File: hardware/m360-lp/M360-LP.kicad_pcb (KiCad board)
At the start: 2 copper layers, 0 parts

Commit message: feat(hardware): footprints da família e posicionamento da M360-LP na caixa
Biblioteca hardware/lib/M360.pretty com os quatro footprints que faltavam: Pro Mini,
soquete do mezanino, RJ45 (C385834) e reed (C315909). Os dois últimos vieram do LCSC pelo
easyeda2kicad, com os pinos-guia do RJ45 corrigidos para furo não metalizado e o modelo 3D
subido 6,3 mm — vinha atravessando a placa. O datasheet confirma conector comum: corpo de
12,6 mm apoiado na face e pinos de 3,0 mm.

O soquete do mezanino não precisa ser espelhado: o PinSocket stock já tem a coluna par em x
negativo, o mesmo lado em que ela fica no J1 do mezanino, que é montado na face de baixo.
Esquemático e documento corrigidos.

Furos livres do Pro Mini medidos por foto (docs/prominiFront.jpg), por homografia a partir
de quatro pinos de canto de posição conhecida (passo 2,54 mm, fileiras a 15,24 mm; escala
consistente em 2% nas quatro bordas): A5 em (12,70; 8,89), A4 em (12,70; 11,43) e GND/A6/A7
em x = 7,62/10,16/12,70 com y = 28,3 ± 0,3. Os espaçamentos medidos (2,57 e 2,59 mm)
confirmam a grade de 2,54. Esses cinco furos levam 1,2 mm — e não 1,0 — para absorver a
incerteza da medição; confirmar com paquímetro antes de fabricar.

Posicionamento em 86 × 62 mm, formato imposto pela caixa de 100 × 100 × 50 mm: o plugue
RJ45 é crimpado dentro da caixa e pede ~25-30 mm livres à frente dos conectores, com os
prensa-cabos na parede em frente. RJ45 e reed na borda de baixo, TVS logo atrás deles,
matriz RC dos 8 canais no meio, Pro Mini deitado com o header FTDI para fora da borda
esquerda, mezanino no alto à direita com o SMA pela borda e a alimentação embaixo dele
(~11 mm livres, só SMD baixo). DRC sem sobreposição de courtyard nem erro de isolamento;
faltam o roteamento e o acerto de serigrafia dos textos de U2, U4 e U5.

Co-Authored-By: Claude Opus 5 (1M context) <noreply@anthropic.com>
Claude-Session: https://claude.ai/code/session_01G3CpSsqAsoKgMUYE5MhRV7
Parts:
- added A1: Pro Mini 3V3 8MHz, M360:Arduino_ProMini_DeeKRobot, F.Cu at (112.0, 121.0)
- added C1: 1uF, Capacitor_SMD:C_0603_1608Metric, F.Cu at (169.5, 104.0)
- added C10: 100nF, Capacitor_SMD:C_0603_1608Metric, F.Cu at (114.4, 139.5)
- added C11: 100nF, Capacitor_SMD:C_0603_1608Metric, F.Cu at (118.6, 139.5)
- added C12: 100nF, Capacitor_SMD:C_0603_1608Metric, F.Cu at (122.8, 139.5)
- added C13: 100nF, Capacitor_SMD:C_0603_1608Metric, F.Cu at (127.0, 139.5)
- added C14: 100nF, Capacitor_SMD:C_0603_1608Metric, F.Cu at (131.2, 139.5)
- added C15: 100nF, Capacitor_SMD:C_0603_1608Metric, F.Cu at (135.4, 139.5)
- added C2: 1uF, Capacitor_SMD:C_0603_1608Metric, F.Cu at (178.0, 104.0)
- added C3: 10uF, Capacitor_SMD:C_0805_2012Metric, F.Cu at (165.0, 116.0)
- added C4: 100nF, Capacitor_SMD:C_0603_1608Metric, F.Cu at (142.0, 125.5)
- added C5: 10nF, Capacitor_SMD:C_0603_1608Metric, F.Cu at (172.5, 110.0)
- added C6: 1uF, Capacitor_SMD:C_0603_1608Metric, F.Cu at (178.5, 110.0)
- added C7: 100nF, Capacitor_SMD:C_0603_1608Metric, F.Cu at (147.0, 105.5)
- added C8: 100nF, Capacitor_SMD:C_0603_1608Metric, F.Cu at (106.0, 139.5)
- added C9: 100nF, Capacitor_SMD:C_0603_1608Metric, F.Cu at (110.2, 139.5)
- added H1: MountingHole_3.2mm_M3, MountingHole_3.2mm_M3, F.Cu at (103.5, 103.5)
- added H2: MountingHole_3.2mm_M3, MountingHole_3.2mm_M3, F.Cu at (182.5, 128.0)
- added H3: MountingHole_3.2mm_M3, MountingHole_3.2mm_M3, F.Cu at (103.5, 158.5)
- added H4: MountingHole_3.2mm_M3, MountingHole_3.2mm_M3, F.Cu at (182.5, 158.5)
- added J1: RJ45 SOLO, M360:RJ45_R-RJ45R08P-A004, F.Cu at (116.0, 153.3)
- added J2: RJ45 CLIMA/AUX, M360:RJ45_R-RJ45R08P-A004, F.Cu at (134.0, 153.3)
- added J3: J_VIN 3,0-6V, Connector_JST:JST_XH_B2B-XH-A_1x02_P2.50mm_Vertical, F.Cu at (178.0, 140.0)
- added J4: M360-RF, M360:M360-RF_Soquete_2x05, F.Cu at (158.8, 107.4)
- added Q1: AO3401A, Package_TO_SOT_SMD:SOT-23, F.Cu at (165.0, 104.0)
- added Q2: AO3401A, Package_TO_SOT_SMD:SOT-23, F.Cu at (165.0, 110.0)
- added R1: 2M, Resistor_SMD:R_0603_1608Metric, F.Cu at (134.0, 125.5)
- added R10: 10k, Resistor_SMD:R_0603_1608Metric, F.Cu at (122.8, 129.5)
- added R11: 10k, Resistor_SMD:R_0603_1608Metric, F.Cu at (127.0, 129.5)
- added R12: 10k, Resistor_SMD:R_0603_1608Metric, F.Cu at (131.2, 129.5)
- added R13: 10k, Resistor_SMD:R_0603_1608Metric, F.Cu at (135.4, 129.5)
- added R14: 1k, Resistor_SMD:R_0603_1608Metric, F.Cu at (106.0, 134.5)
- added R15: 1k, Resistor_SMD:R_0603_1608Metric, F.Cu at (110.2, 134.5)
- added R16: 1k, Resistor_SMD:R_0603_1608Metric, F.Cu at (114.4, 134.5)
- added R17: 1k, Resistor_SMD:R_0603_1608Metric, F.Cu at (118.6, 134.5)
- added R18: 1k, Resistor_SMD:R_0603_1608Metric, F.Cu at (122.8, 134.5)
- added R19: 1k, Resistor_SMD:R_0603_1608Metric, F.Cu at (127.0, 134.5)
- added R2: 1M, Resistor_SMD:R_0603_1608Metric, F.Cu at (138.0, 125.5)
- added R20: 1k, Resistor_SMD:R_0603_1608Metric, F.Cu at (131.2, 134.5)
- added R21: 1k, Resistor_SMD:R_0603_1608Metric, F.Cu at (135.4, 134.5)
- added R22: 4.7k, Resistor_SMD:R_0603_1608Metric, F.Cu at (155.0, 130.0)
- added R23: 10k, Resistor_SMD:R_0603_1608Metric, F.Cu at (159.0, 130.0)
- added R24: 3.3k, Resistor_SMD:R_0603_1608Metric, F.Cu at (163.0, 130.0)
- added R25: 3.3k, Resistor_SMD:R_0603_1608Metric, F.Cu at (167.0, 130.0)
- added R3: 10k, Resistor_SMD:R_0603_1608Metric, F.Cu at (147.0, 118.5)
- added R4: 100k, Resistor_SMD:R_0603_1608Metric, F.Cu at (169.5, 110.0)
- added R5: 10k, Resistor_SMD:R_0603_1608Metric, F.Cu at (175.5, 110.0)
- added R6: 10k, Resistor_SMD:R_0603_1608Metric, F.Cu at (106.0, 129.5)
- added R7: 10k, Resistor_SMD:R_0603_1608Metric, F.Cu at (110.2, 129.5)
- added R8: 10k, Resistor_SMD:R_0603_1608Metric, F.Cu at (114.4, 129.5)
- added R9: 10k, Resistor_SMD:R_0603_1608Metric, F.Cu at (118.6, 129.5)
- added SW1: Reed, M360:Reed_Littelfuse_59170, F.Cu at (160.0, 158.0)
- added U1: MCP1700T-3302E/TT, Package_TO_SOT_SMD:SOT-23, F.Cu at (174.0, 104.0)
- added U2: 74HC4051, Package_SO:SOIC-16_3.9x9.9mm_P1.27mm, F.Cu at (147.0, 112.0)
- added U3: SRV05-4, Package_TO_SOT_SMD:SOT-23-6, F.Cu at (112.0, 143.5)
- added U4: SRV05-4, Package_TO_SOT_SMD:SOT-23-6, F.Cu at (124.0, 143.5)
- added U5: SRV05-4, Package_TO_SOT_SMD:SOT-23-6, F.Cu at (136.0, 143.5)
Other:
- board outline added: 86 x 62 mm

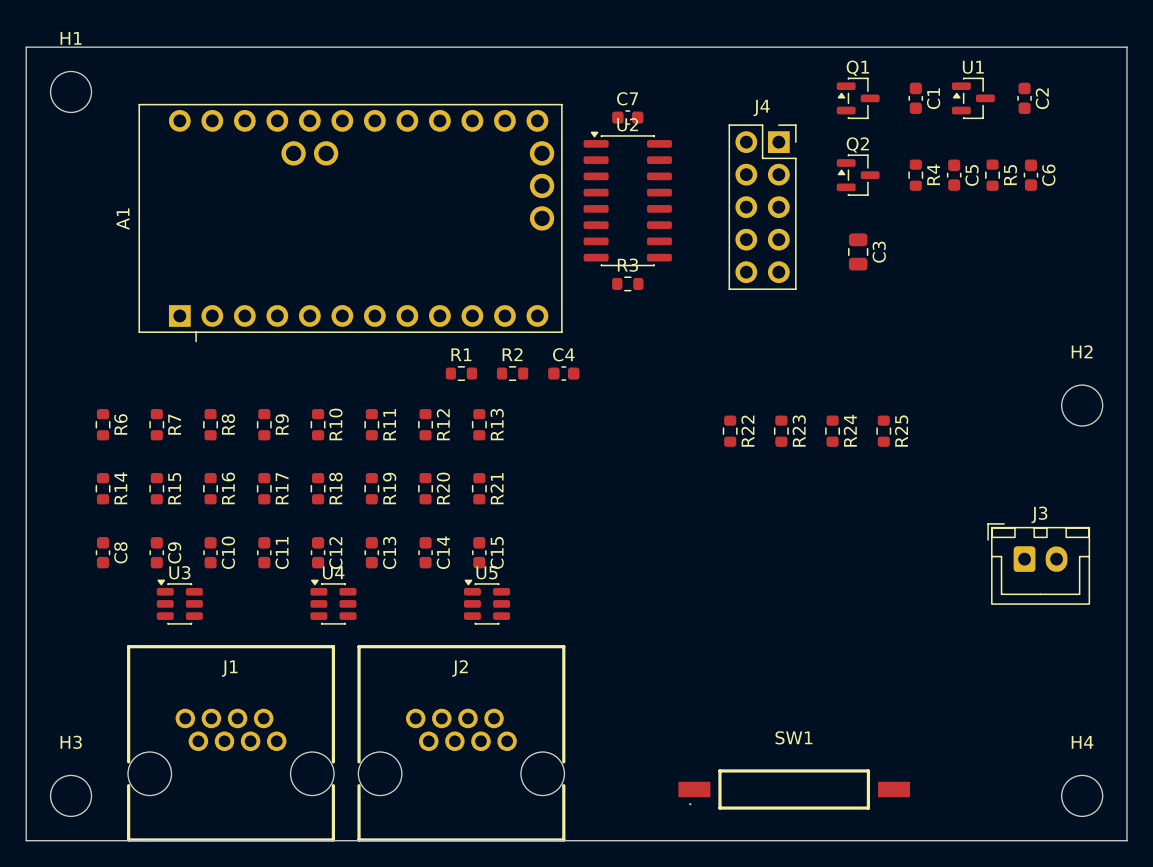
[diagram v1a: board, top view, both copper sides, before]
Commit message: feat(hardware): roteamento e planos de terra da M360-LP
Regras da placa antes de rotear: isolamento 0,2 mm, trilha 0,25 mm e via 0,6/0,3 mm
(estavam em isolamento 0 e trilha 0,2).

Roteamento pelo Freerouting 1.9.0, chamado direto na linha de comando: o autoroute do MCP
exige Java 21 ou Docker em execução, e aqui há Java 17 — que basta para a versão 1.9.
Fluxo: export DSN pelo MCP, `java -jar freerouting.jar -de ... -do ... -mp 20`, import SES
pelo MCP. Resultado: 552 trilhas e 48 vias, com a otimização melhorando o desenho em ~51%.
**Zero ligações pendentes** (eram 135) e nenhuma violação de isolamento.

Planos de terra (GND) nas duas faces, isolamento de 0,25 mm, preenchidos com
`kicad-cli pcb drc --refill-zones --save-board` — o refill_zones do MCP é o que arrisca
falha de segmentação.

Dois erros de haste térmica insuficiente apareceram com o preenchimento e foram corrigidos:
- hastes de 0,35 mm com folga de 0,3 mm (eram 0,5/0,5), que cabem no anel apertado dos pads
  THT e preservam o alívio térmico para a solda manual — resolveu o pino 10 do J4;
- ligação sólida no pino 8 do J2 (GND do RJ45), onde o campo de pinos escalonados de
  1,02 mm não deixa espaço para duas hastes. É o pad de terra do chicote: ligação sólida dá
  o melhor retorno de massa, ao custo de mais calor na solda desse pad.

Restam apenas avisos de serigrafia: a frente dos RJ45 rente à borda (proposital) e textos de
referência de U2, U4 e U5 sobre ilhas — acerto cosmético pendente.

Co-Authored-By: Claude Opus 5 (1M context) <noreply@anthropic.com>
Claude-Session: https://claude.ai/code/session_01G3CpSsqAsoKgMUYE5MhRV7
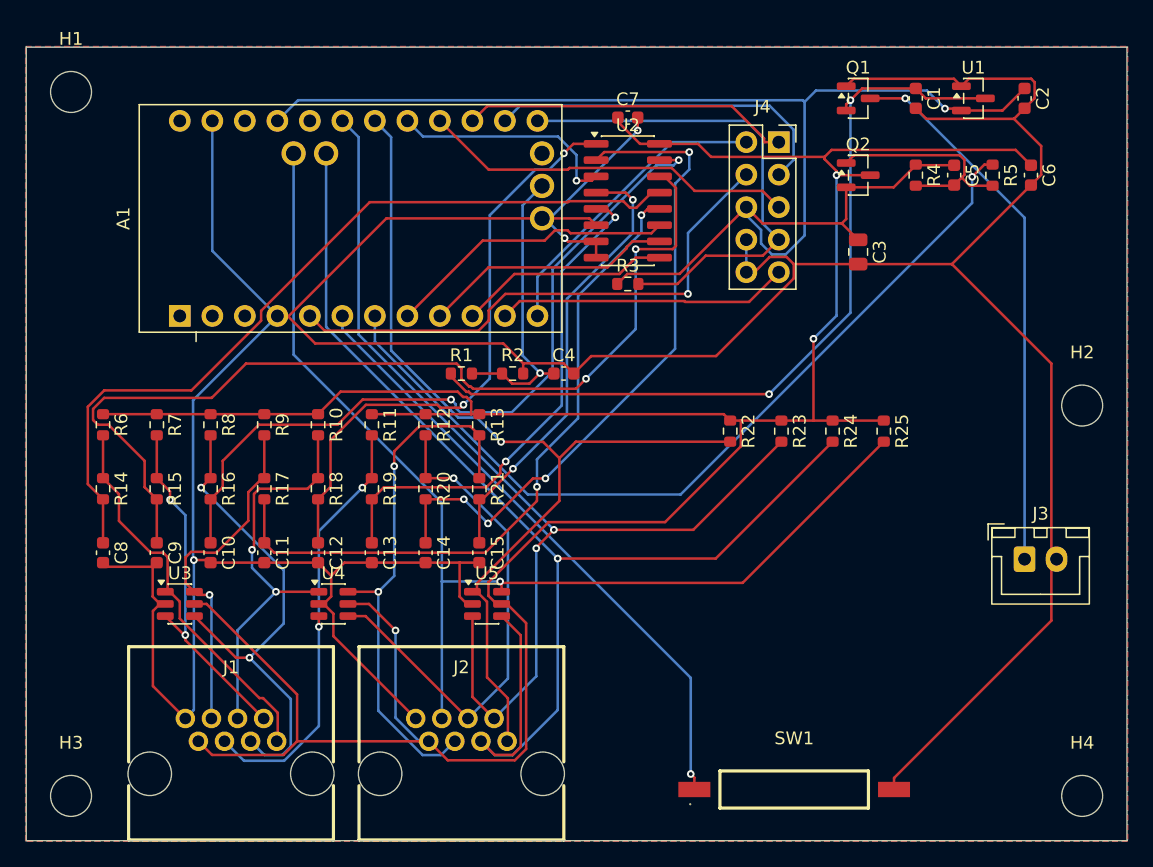
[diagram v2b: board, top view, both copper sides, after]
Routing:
- net GND: track 0.00 -> 315.2 mm, vias 0 -> 3
- net VSW: track 0.00 -> 227.5 mm, vias 0 -> 3
- net 3V3: track 0.00 -> 113.5 mm, vias 0 -> 1
- net SDA: track 0.00 -> 98.8 mm, vias 0 -> 1
- net SCL: track 0.00 -> 88.8 mm, vias 0 -> 1
- net DHT: track 0.00 -> 84.8 mm, vias 0 -> 2
- net SOIL1_F: track 0.00 -> 75.8 mm, vias 0 -> 2
- net ONEWIRE: track 0.00 -> 75.1 mm, vias 0 -> 1
- net VSW_EN: track 0.00 -> 67.1 mm, vias 0 -> 1
- net SOIL0_F: track 0.00 -> 63.6 mm
- net VIN: track 0.00 -> 63.4 mm, vias 0 -> 2
- net SOIL2_F: track 0.00 -> 59.4 mm, vias 0 -> 2
- net SOIL3_F: track 0.00 -> 54.0 mm, vias 0 -> 2
- net SOIL6_F: track 0.00 -> 52.7 mm, vias 0 -> 4
- net REED: track 0.00 -> 48.4 mm, vias 0 -> 1
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- added copper zone on B.Cu, net GND
- added copper zone on F.Cu, net GND

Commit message: feat(hardware): serigrafia da M360-LP e marca da placa
Os textos de referência de U2, U4 e U5 caíam sobre os pads de C7, C12 e C15, e o do R3 sobre
o contorno de serigrafia do U2 — os oito avisos de componente que sobraram do roteamento. Os
textos foram movidos para a folga livre ao lado de cada peça; nenhum componente mudou de
lugar, então o roteamento não foi tocado:

- U2 vai para a folga entre o corpo e o soquete do mezanino, na vertical;
- U4 e U5 vão para o vão à direita de cada um, entre os TVS e os pull-ups;
- R3 desce para baixo do próprio corpo, saindo do contorno do U2.

Acrescentado "Viridiotech.com.br" na face de cima, no espaço vazio acima do SW1, com 1,5 mm
de altura.

Continuam os oito avisos da frente dos RJ45 rente à borda: são propositais, porque a boca do
conector fica na borda da placa, e a serigrafia ali é aparada na fabricação.

Co-Authored-By: Claude Opus 5 (1M context) <noreply@anthropic.com>
Claude-Session: https://claude.ai/code/session_01G3CpSsqAsoKgMUYE5MhRV7
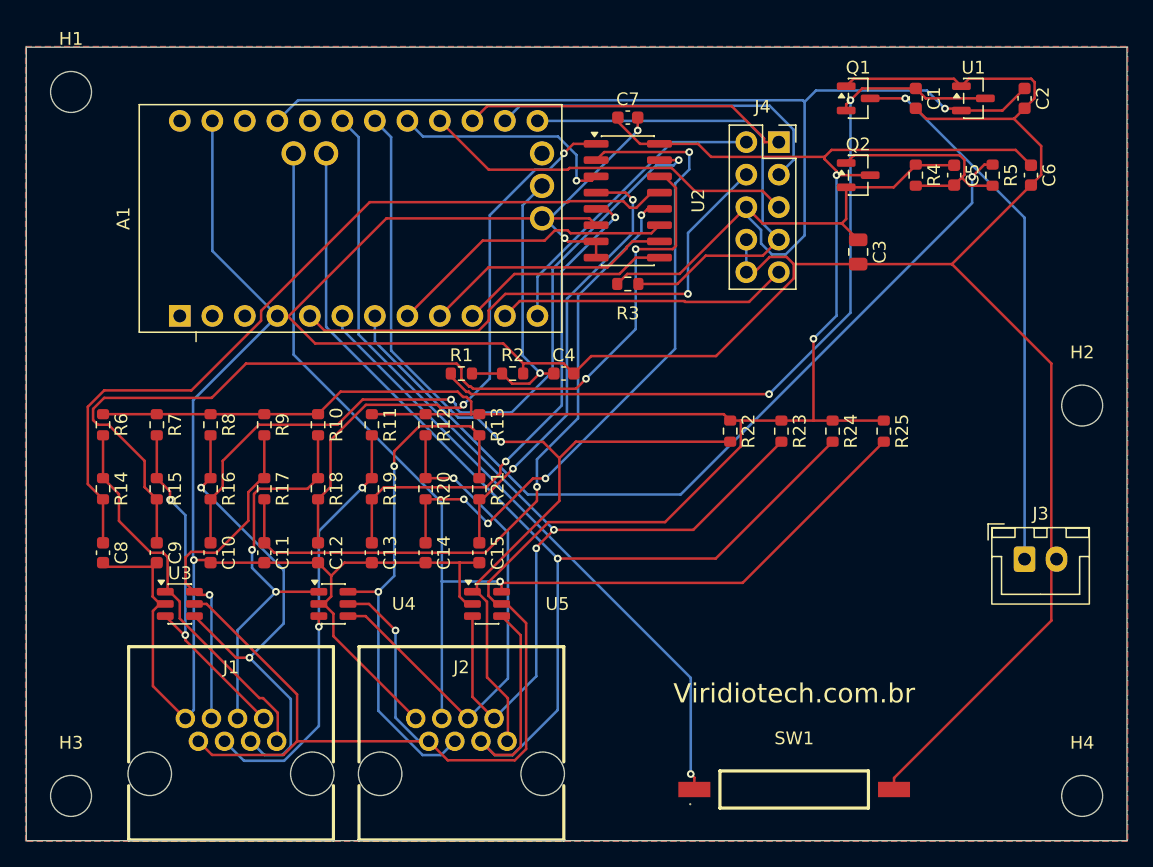
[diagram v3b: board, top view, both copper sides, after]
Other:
- board text added: "Viridiotech.com.br"
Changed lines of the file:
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@@
 		(tags "SOT TO_SOT_SMD")
 		(property "Reference" "U4"
-			(at 0 -2.4 0)
+			(at 5.5 0 0)
 			(layer "F.SilkS")
 			(effects
@@
 		(tags "SOIC SO 16-pin-NSOP R-16 R-16-S D0016A M2B SO16 SOT109-1 751B SOIC_N narrow")
 		(property "Reference" "U2"
-			(at 0 -5.9 0)
+			(at 5.5 0 90)
 			(layer "F.SilkS")
 			(effects
@@
 		(tags "resistor")
 		(property "Reference" "R3"
-			(at 0 -1.43 0)
+			(at 0 2.3 0)
 			(layer "F.SilkS")
 			(effects
@@
 		(tags "SOT TO_SOT_SMD")
 		(property "Reference" "U5"
-			(at 0 -2.4 0)
+			(at 5.5 0 0)
 			(layer "F.SilkS")
 			(effects
@@
 		(layer "Edge.Cuts")
 	)
+	(gr_text "Viridiotech.com.br"
+		(at 160 150.5 0)
+		(layer "F.SilkS")
+		(effects
+			(font
+				(size 1.5 1.5)
+				(thickness 0.25)
+			)
+		)
+	)
 	(segment

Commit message: feat(hardware): legendas de serigrafia na M360-LP e na M360-ACT
Serigrafia para quem monta e liga a placa, não só para quem a projetou.

**M360-ACT** — o campo Value dos conectores passa a aparecer na serigrafia: "5V do quadro",
"M360-RF", "RJ45 RELES-A", "RJ45 RELES-B" e "RJ45 SENSORES". Sem isso o instalador vê J3, J4 e
J5 e não tem como saber qual chicote vai onde. Mais o nome do modelo abaixo da marca.

**M360-LP** — nome do modelo abaixo da marca, e **VCC/GND nas ilhas do J3**. A entrada de
alimentação é um JST de 2 vias e nada na placa dizia qual é qual; ligar invertido queima o nó,
então a legenda é proteção, não conforto. A polaridade foi conferida na netlist, não deduzida da
ordem dos pinos: pino 1 = /VIN_RAW, pino 2 = GND (mesma rede de C4.2, C6.2, J1.8, J2.8).

Três armadilhas de serigrafia, todas custaram rodada extra e ficaram registradas no README:

- **o campo Value herda a rotação do footprint.** O J1 da ACT está em rot 90, e definir só a
  posição deixou "5V do quadro" na vertical, atravessando a própria ilha do borne
  (`silk_over_copper`). É preciso forçar o ângulo;
- **afastar um rótulo de uma ilha empurrando-o para a borda troca um problema por outro.** Ao
  tirar esse mesmo texto de cima da ilha, mandei-o para x = 99 — a placa começa em x = 100, e
  entraram um `silk_edge_clearance` e dois `silk_overlap`;
- **o DRC não pega tudo.** As legendas dos RJ45 na faixa de 2,5 mm entre os TVS e os conectores
  passavam no DRC e ficavam ilegíveis sobre os corpos. Só a inspeção da imagem mostrou; subiram
  para acima da fileira de TVS.

Verificação: LP com 8 violações e ACT com 13, todas `silk_edge_clearance` das frentes dos RJ45
rente à borda — intencionais e já registradas nos commits de roteamento. **0 itens desconectados
nas duas**, ou seja, nada de elétrico foi tocado.

Co-Authored-By: Claude Opus 5 (1M context) <noreply@anthropic.com>
Claude-Session: https://claude.ai/code/session_01G3CpSsqAsoKgMUYE5MhRV7
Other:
- board text added: "GND"
- board text added: "M360-LP"
- board text added: "VCC"
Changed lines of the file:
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@@
 		(layer "Edge.Cuts")
 	)
-	(gr_text "Viridiotech.com.br"
-		(at 160 150.5 0)
+	(gr_text "VCC"
+		(at 177 135 0)
 		(layer "F.SilkS")
 		(effects
+			(font
+				(size 0.8 0.8)
+				(thickness 0.15)
+			)
+		)
+	)
+	(gr_text "GND"
+		(at 181.5 135 0)
+		(layer "F.SilkS")
+		(effects
+			(font
+				(size 0.8 0.8)
+				(thickness 0.15)
+			)
+		)
+	)
+	(gr_text "Viridiotech.com.br"
+		(at 158 147 0)
+		(layer "F.SilkS")
+		(effects
+			(font
+				(size 1.5 1.5)
+				(thickness 0.25)
+			)
+		)
+	)
+	(gr_text "M360-LP"
+		(at 158 150.5 0)
+		(layer "F.SilkS")
+		(effects
